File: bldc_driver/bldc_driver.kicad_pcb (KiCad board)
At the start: 2 copper layers, 46.4 x 26.5 mm, 84 parts, among them CON1 SAM-SWD-10, J1 I2C 1, Q1 PSMN0R925YLC, Q2 PSMN0R925YLC, Q3 PSMN0R925YLC, Q4 PSMN0R925YLC, Q5 PSMN0R925YLC, Q6 PSMN0R925YLC, U1 SAMD21E16L-MU, U2 INA199C2, U3 MIC4609

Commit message: bldc pdb
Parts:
- removed the REF** at (159.9, 83.2)
- removed the REF** at (148.6, 77.6)
- removed the REF** at (150.1, 82.9)
- removed the REF** at (140.3, 73.7)
- removed the REF** at (159.9, 77.5)
- removed the REF** at (159.8, 88.8)
- removed the REF** at (150.4, 88.1)
- removed the REF** at (150.4, 91.1)
- removed the REF** at (150.4, 85.6)
- removed the REF** at (150.4, 80.9)
- removed the REF** at (150.9, 75.4)
- removed the REF** at (148.6, 74.2)
- added R33: 10k, Resistor_SMD:R_0603_1608Metric_Pad1.05x0.95mm_HandSolder, F.Cu at (129.7, 83.6)
- added REF**: TestPoint_Pad_1.5x1.5mm, TestPoint:TestPoint_Pad_1.5x1.5mm, B.Cu at (123.3, 74.2)
- added REF**: TestPoint_Pad_1.5x1.5mm, TestPoint:TestPoint_Pad_1.5x1.5mm, B.Cu at (150.1, 91.1)
- added REF**: TestPoint_Pad_1.5x1.5mm, TestPoint:TestPoint_Pad_1.5x1.5mm, B.Cu at (159.9, 77.5)
- added REF**: TestPoint_Pad_1.5x1.5mm, TestPoint:TestPoint_Pad_1.5x1.5mm, B.Cu at (159.9, 83.2)
- added REF**: TestPoint_Pad_1.5x1.5mm, TestPoint:TestPoint_Pad_1.5x1.5mm, B.Cu at (159.8, 88.8)
- added REF**: TestPoint_Pad_1.5x1.5mm, TestPoint:TestPoint_Pad_1.5x1.5mm, B.Cu at (140.2, 73.7)
- added REF**: TestPoint_Pad_1.5x1.5mm, TestPoint:TestPoint_Pad_1.5x1.5mm, B.Cu at (151.4, 75.4)
- added REF**: TestPoint_Pad_1.5x1.5mm, TestPoint:TestPoint_Pad_1.5x1.5mm, B.Cu at (148.7, 74.2)
- added REF**: TestPoint_Pad_1.5x1.5mm, TestPoint:TestPoint_Pad_1.5x1.5mm, B.Cu at (148.7, 78.4)
- added REF**: TestPoint_Pad_1.5x1.5mm, TestPoint:TestPoint_Pad_1.5x1.5mm, B.Cu at (150.1, 80.9)
- added REF**: TestPoint_Pad_1.5x1.5mm, TestPoint:TestPoint_Pad_1.5x1.5mm, B.Cu at (150.1, 83.1)
- added REF**: TestPoint_Pad_1.5x1.5mm, TestPoint:TestPoint_Pad_1.5x1.5mm, B.Cu at (150.1, 85.6)
- added REF**: TestPoint_Pad_1.5x1.5mm, TestPoint:TestPoint_Pad_1.5x1.5mm, B.Cu at (150.1, 88.1)
- C1, C2: footprint Capacitors_SMD:C_0805_HandSoldering -> Capacitor_SMD:C_0805_2012Metric_Pad1.15x1.40mm_HandSolder
- C10, C11, C12, C13, C14, C15, C16, C3, C4, C5, C7, C8, C9: footprint Capacitors_SMD:C_0603_HandSoldering -> Capacitor_SMD:C_0603_1608Metric_Pad1.05x0.95mm_HandSolder
- C17, C18, C19: value 1nF -> 22nF; footprint Capacitors_SMD:C_0603_HandSoldering -> Capacitor_SMD:C_0603_1608Metric_Pad1.05x0.95mm_HandSolder
- CON1: footprint Pin_Headers:Pin_Header_Straight_2x05_Pitch2.54mm -> Connector_PinHeader_2.54mm:PinHeader_2x05_P2.54mm_Vertical
- D1, D2, D3: footprint LEDs:LED_0603_HandSoldering -> LED_SMD:LED_0603_1608Metric_Pad1.05x0.95mm_HandSolder
- D4, D5, D6, D7, D8, D9: footprint Diodes_SMD:D_SOD-323_HandSoldering -> Diode_SMD:D_SOD-323_HandSoldering
- J1: footprint Pin_Headers:Pin_Header_Straight_1x04_Pitch2.54mm -> Connector_PinHeader_2.54mm:PinHeader_1x04_P2.54mm_Vertical
- L1: footprint Inductors_SMD:L_0805_HandSoldering -> Inductor_SMD:L_0805_2012Metric_Pad1.15x1.40mm_HandSolder
- L2: footprint Inductors_SMD:L_0603_HandSoldering -> Inductor_SMD:L_0603_1608Metric_Pad1.05x0.95mm_HandSolder
- R1, R10, R12, R13, R14, R15, R16, R17, R18, R19, R2, R20, R21, R22, R23, R24, R25, R26, R27, R28, R29, R3, R30, R4, R7, R9: footprint Resistors_SMD:R_0603_HandSoldering -> Resistor_SMD:R_0603_1608Metric_Pad1.05x0.95mm_HandSolder
- R11: footprint Resistors_SMD:R_2512_HandSoldering -> Resistor_SMD:R_2512_6332Metric_Pad1.52x3.35mm_HandSolder
- R5, R6, R8: value 3k -> 100k; footprint Resistors_SMD:R_0603_HandSoldering -> Resistor_SMD:R_0603_1608Metric_Pad1.05x0.95mm_HandSolder
- U1: footprint Housings_QFP:TQFP-32_7x7mm_Pitch0.8mm -> Package_QFP:TQFP-32_7x7mm_P0.8mm
- moved D6 1.91 mm to (153.7, 79.2)
- moved R30 0.39 mm to (128.0, 82.2)
- moved R13 0.38 mm to (152.1, 77.6)
- moved L1 0.27 mm to (125.1, 88.4)
- moved C1 0.13 mm to (127.8, 87.3)
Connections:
- U1 pad 1: /bldc_unit1/MOTOR_A -> Net-(U1-Pad1)
- U1 pad 2: /bldc_unit1/MOTOR_ZERO -> Net-(U1-Pad2)
- U1 pad 3: Net-(U1-Pad3) -> /bldc_unit1/MOTOR_A
- U1 pad 4: Net-(U1-Pad4) -> /bldc_unit1/MOTOR_ZERO
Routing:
- net /+3.3V: track 71.4 -> 78.4 mm
- net /+V_MOTOR: track 93.2 -> 88.1 mm
- net GND: track 68.2 -> 69.8 mm, vias 8 -> 26
- net /bldc_unit1/MOTOR_ZERO: track 14.1 -> 12.6 mm
- net /bldc_unit1/MOTOR_A: track 21.8 -> 20.3 mm
- net /RESET: track 18.8 -> 20.1 mm
- net Net-(C8-Pad1): track 11.7 -> 10.6 mm
- net /bldc_unit1/GLA: track 1.90 -> 2.78 mm
- net Net-(C8-Pad2): track 6.40 -> 5.64 mm
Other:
- board text added: "BLDC 20A V1.2 2019 Acshi Haggenmiller"
- board text removed: "BLDC 20A V1.1 2018 Acshi Haggenmiller"

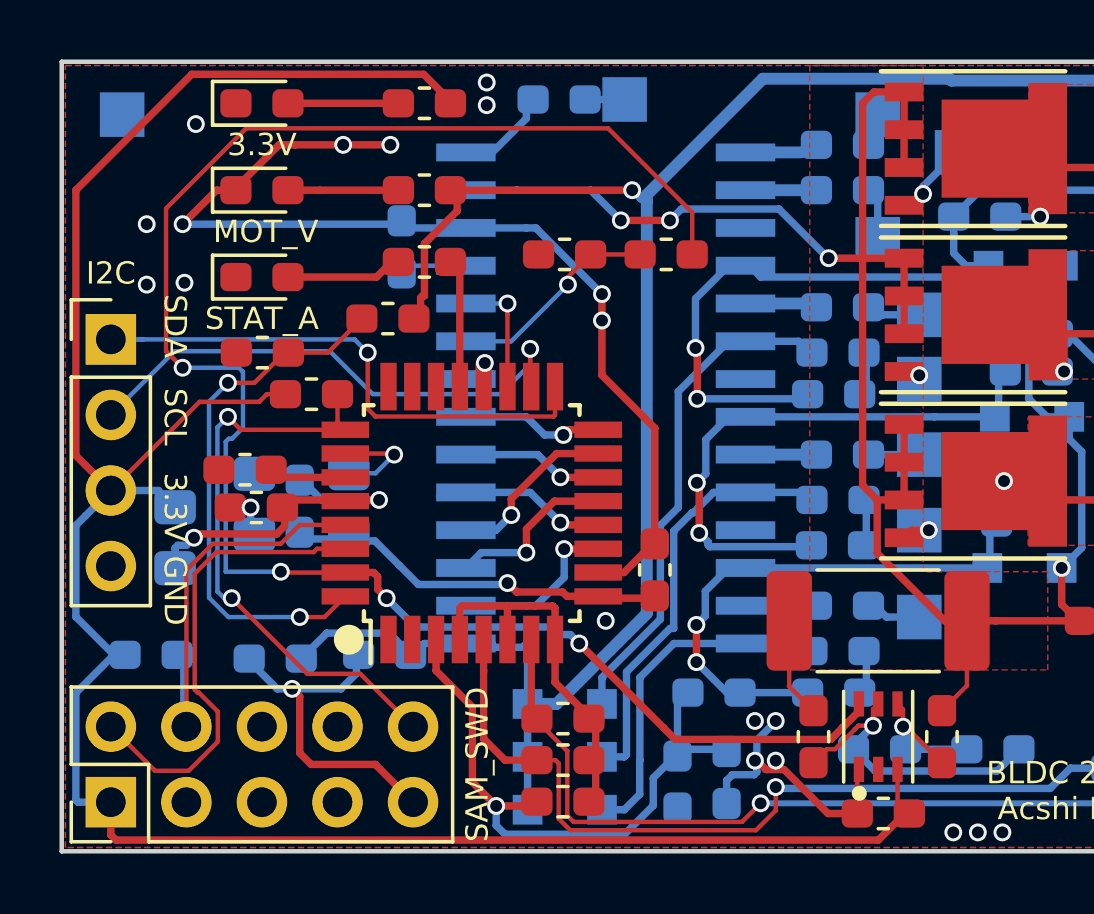
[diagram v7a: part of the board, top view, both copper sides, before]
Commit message: basic rerouting of new atmega chip on pcb; needs better grounding, more coupling across the two sides, since the ground is a bit tenuous
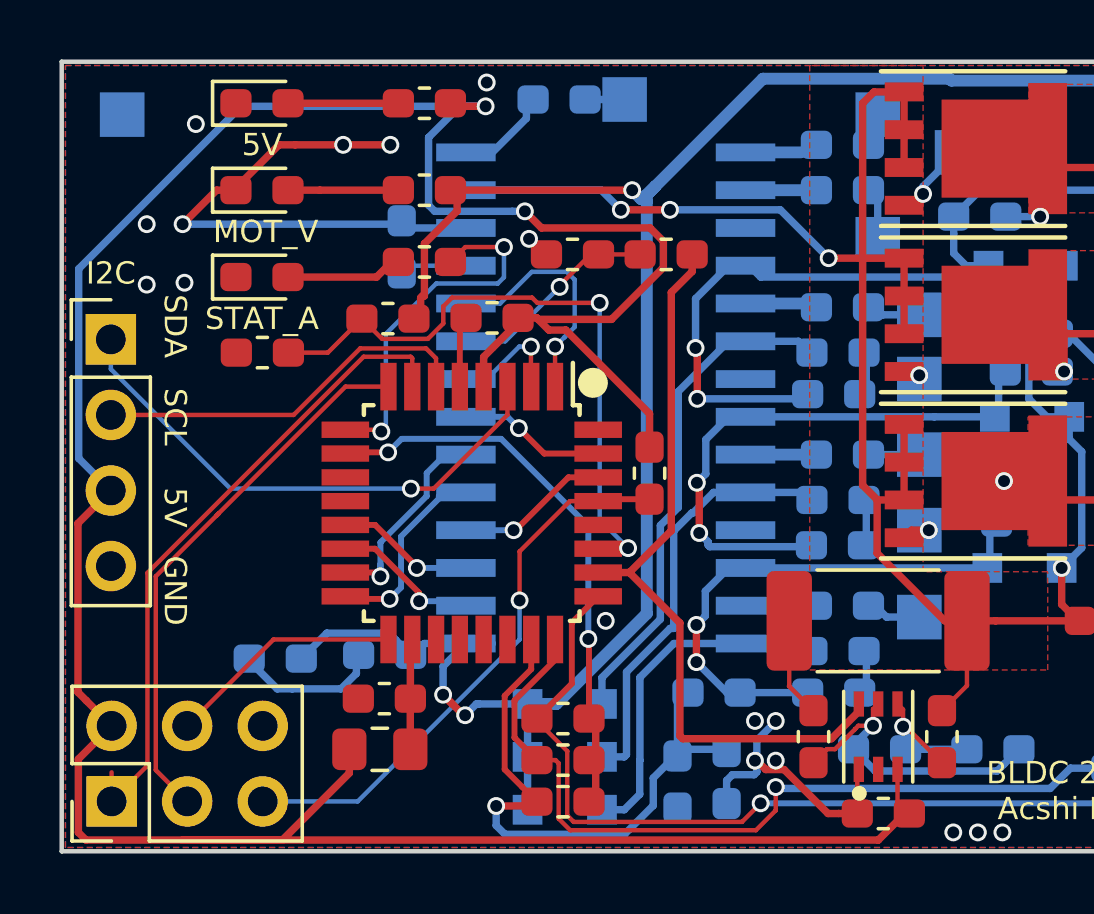
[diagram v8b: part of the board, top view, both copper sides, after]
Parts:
- removed C3, C5: 100nF, Capacitor_SMD:C_0603_1608Metric_Pad1.05x0.95mm_HandSolder
- removed C4: 1uF, Capacitor_SMD:C_0603_1608Metric_Pad1.05x0.95mm_HandSolder
- removed CON1: SAM-SWD-10, Connector_PinHeader_2.54mm:PinHeader_2x05_P2.54mm_Vertical
- removed L2: Ferrite_Bead_Small, Inductor_SMD:L_0603_1608Metric_Pad1.05x0.95mm_HandSolder
- removed R4: 3k, Resistor_SMD:R_0603_1608Metric_Pad1.05x0.95mm_HandSolder
- added J2: AVR-ISP-6, Connector_PinHeader_2.54mm:PinHeader_2x03_P2.54mm_Vertical, F.Cu at (123.0, 97.3)
- C1, C2: value 10uF -> 100nF; footprint Capacitor_SMD:C_0805_2012Metric_Pad1.15x1.40mm_HandSolder -> Capacitor_SMD:C_0603_1608Metric_Pad1.05x0.95mm_HandSolder; moved to F.Cu
- C14, C15, C16: value 0.68uF -> 1uF 50V
- L1: moved to F.Cu
- R1: value 470R -> 1k
- R14, R15, R16: value 4.7R -> 200R
- R17, R18, R19: value 4.7R -> 10R
- R31: value 15K -> 20K
- R32: value 2.2K -> 3K
- U1: value SAMD21E16L-MU -> ATmega328PB-AU
- moved R33 11.7 mm to (141.0, 86.2), turned to 90 degrees
- moved L1 9.90 mm to (132.0, 95.5), turned to 0 degrees
- moved C2 7.89 mm to (135.8, 81.0), turned to 180 degrees
- moved C1 7.86 mm to (132.1, 93.8), turned to 180 degrees
- moved R32 0.27 mm to (138.5, 78.9)
- turned U1 to 270 degrees
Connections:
- C11 pad 2: /+3.3V -> /+5V
- C2 pad 1: Net-(C2-Pad1) -> /+5V
- J1 pad 3: /+3.3V -> /+5V
- L1 pad 1: /+3.3V -> /+5V
- R1 pad 2: /+3.3V -> /+5V
- R33 pad 1: /+3.3V -> /~RESET
- R33 pad 2: /RESET -> /+5V
- U1 pad 1: Net-(U1-Pad1) -> /bldc_unit1/ENABLE
- U1 pad 10: GND -> /bldc_unit1/MOTOR_ZERO
- U1 pad 11: /bldc_unit1/IN_HA -> Net-(U1-Pad11)
- U1 pad 12: /bldc_unit1/IN_LA -> Net-(U1-Pad12)
- U1 pad 14: /bldc_unit1/IN_LB -> /bldc_unit1/IN_HA
- U1 pad 15: /bldc_unit1/IN_HC -> /bldc_unit1/IN_LB
- U1 pad 16: /bldc_unit1/IN_LC -> /bldc_unit1/IN_LA
- U1 pad 17: /SDA -> /MOSI
- U1 pad 18: /SCL -> Net-(C1-Pad1)
- U1 pad 19: /bldc_unit1/ENABLE -> Net-(U1-Pad19)
- U1 pad 2: Net-(U1-Pad2) -> /bldc_unit1/~FAULT
- U1 pad 20: /bldc_unit1/~FAULT -> Net-(U1-Pad20)
- U1 pad 21: /STATUS -> GND
- U1 pad 23: Net-(U1-Pad23) -> /bldc_unit1/MOTOR_A
- U1 pad 24: Net-(U1-Pad24) -> /bldc_unit1/MOTOR_B
- U1 pad 25: /RESET -> /bldc_unit1/MOTOR_C
- U1 pad 26: GND -> /bldc_unit1/CURRENT
- U1 pad 27: Net-(C4-Pad1) -> Net-(R29-Pad2)
- U1 pad 28: Net-(C1-Pad1) -> Net-(U1-Pad28)
- U1 pad 29: /SWCLK -> /~RESET
- U1 pad 3: /bldc_unit1/MOTOR_A -> /SDA
- U1 pad 30: /SWDIO -> /bldc_unit1/IN_HC
- U1 pad 31: /bldc_unit1/CURRENT -> /bldc_unit1/IN_LC
- U1 pad 32: Net-(R29-Pad2) -> Net-(U1-Pad32)
- U1 pad 4: /bldc_unit1/MOTOR_ZERO -> /+5V
- U1 pad 5: /bldc_unit1/MOTOR_B -> GND
- U1 pad 6: /bldc_unit1/MOTOR_ZERO -> /SCL
- U1 pad 7: /bldc_unit1/MOTOR_C -> /MISO
- U1 pad 8: /bldc_unit1/MOTOR_ZERO -> /SCK
- U1 pad 9: Net-(C2-Pad1) -> /STATUS
- U2 pad 3: /+3.3V -> /+5V
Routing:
- net /+5V: track 0.00 -> 104.3 mm, vias 0 -> 2
- net /+3.3V: track 78.4 -> 0.00 mm
- net /bldc_unit1/CURRENT: track 60.6 -> 25.5 mm, vias 4 -> 0
- net GND: track 69.8 -> 44.8 mm, vias 26 -> 21
- net /MISO: track 0.00 -> 22.5 mm, vias 0 -> 1
- net /RESET: track 20.1 -> 0.00 mm, vias 2 -> 0
- net /~RESET: track 0.00 -> 18.9 mm, vias 0 -> 1
- net /SCK: track 0.00 -> 18.6 mm
- net /SWDIO: track 16.0 -> 0.00 mm
- net /SWCLK: track 14.0 -> 0.00 mm
- net Net-(C2-Pad1): track 12.8 -> 0.00 mm, vias 1 -> 0
- net Net-(C1-Pad1): track 13.2 -> 3.72 mm, vias 2 -> 0
- net /STATUS: track 4.23 -> 12.4 mm, vias 0 -> 2
- net /MOSI: track 0.00 -> 7.97 mm
- net /bldc_unit1/MOTOR_ZERO: track 12.6 -> 19.0 mm, vias 0 -> 2
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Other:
- board text added: "5V"
- board text removed: "3.3V"
- board text removed: "SAM_SWD"
